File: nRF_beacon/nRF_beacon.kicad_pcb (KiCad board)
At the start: 4 copper layers, 60 x 90 mm, 69 parts, among them J1 Conn_02x05_Odd_Even, J2 Conn_02x03_Counter_Clockwise, U1 nRF54L15-QFAA, U2 NPM1300-QEAA-R7, U3 MAX98357A, U4 12BHC186P1-GR, X1 32MHz, X2 32.768 kHz

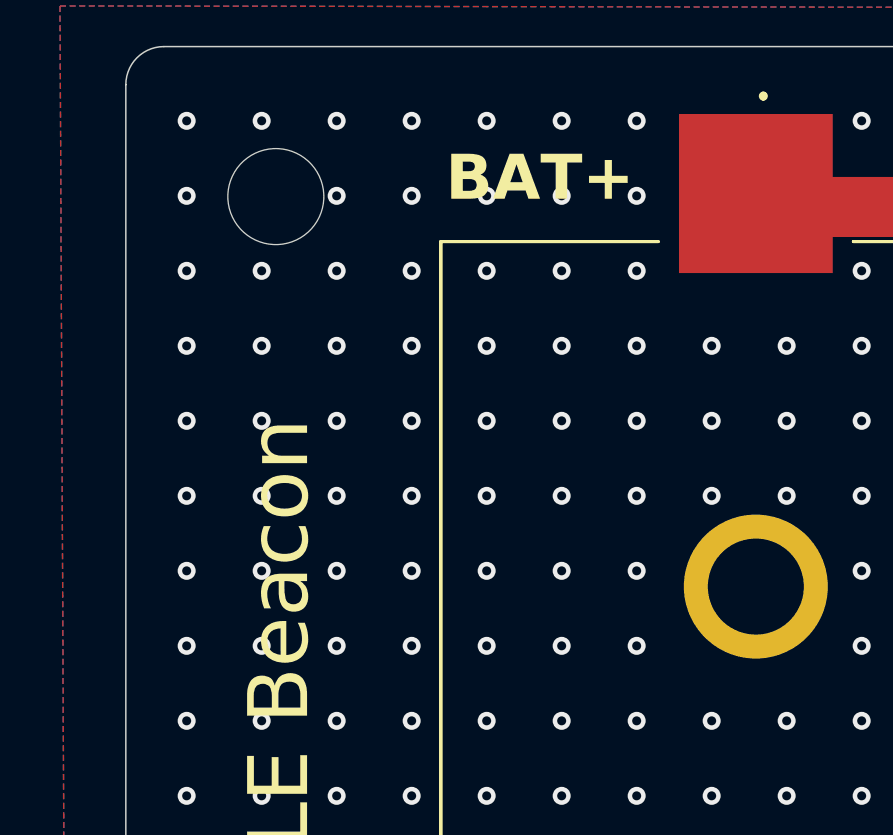
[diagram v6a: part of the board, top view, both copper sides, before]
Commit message: Added silkscreen braille, blind person logo and revision
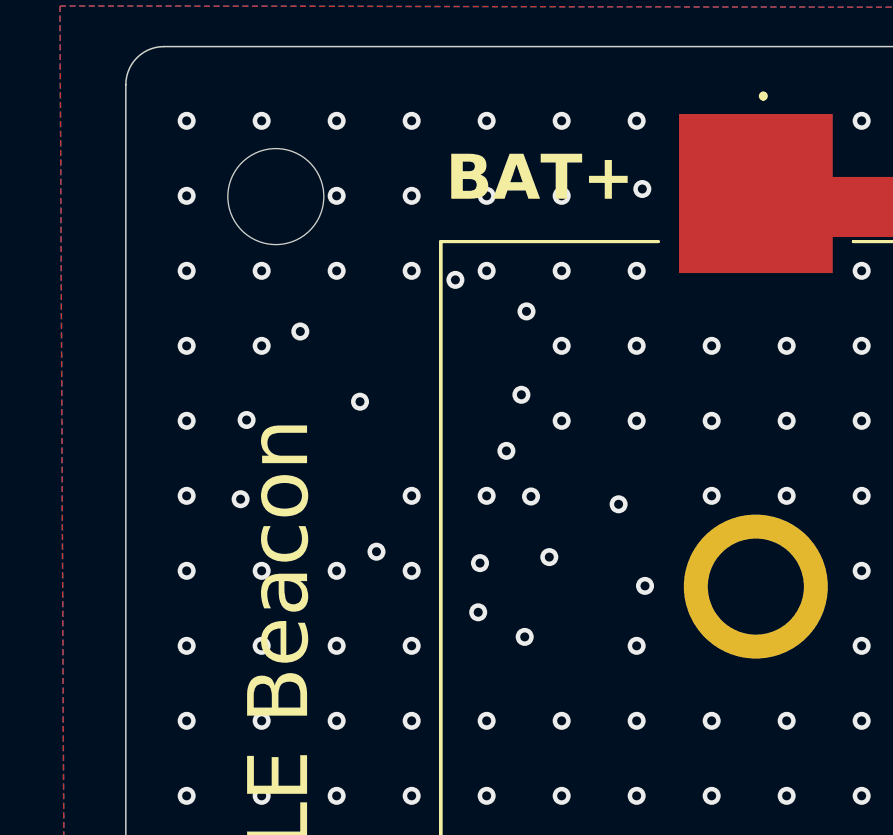
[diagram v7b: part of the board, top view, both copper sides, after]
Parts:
- added G***: LOGO, Ekse:blind, F.Cu at (147.8, 93.4)
- added G***: LOGO, Ekse:ble_sound_beacon_braille, F.Cu at (176.0, 100.0)
- added G***: LOGO, Ekse:høyttaler, F.Cu at (130.9, 69.8)
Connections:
- X1 pad 2: GND -> (no net)
- X1 pad 4: GND -> (no net)
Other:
- board text added: "BLE SOUND BEACON"
- board text added: "Layout by: Mathias Ekse"

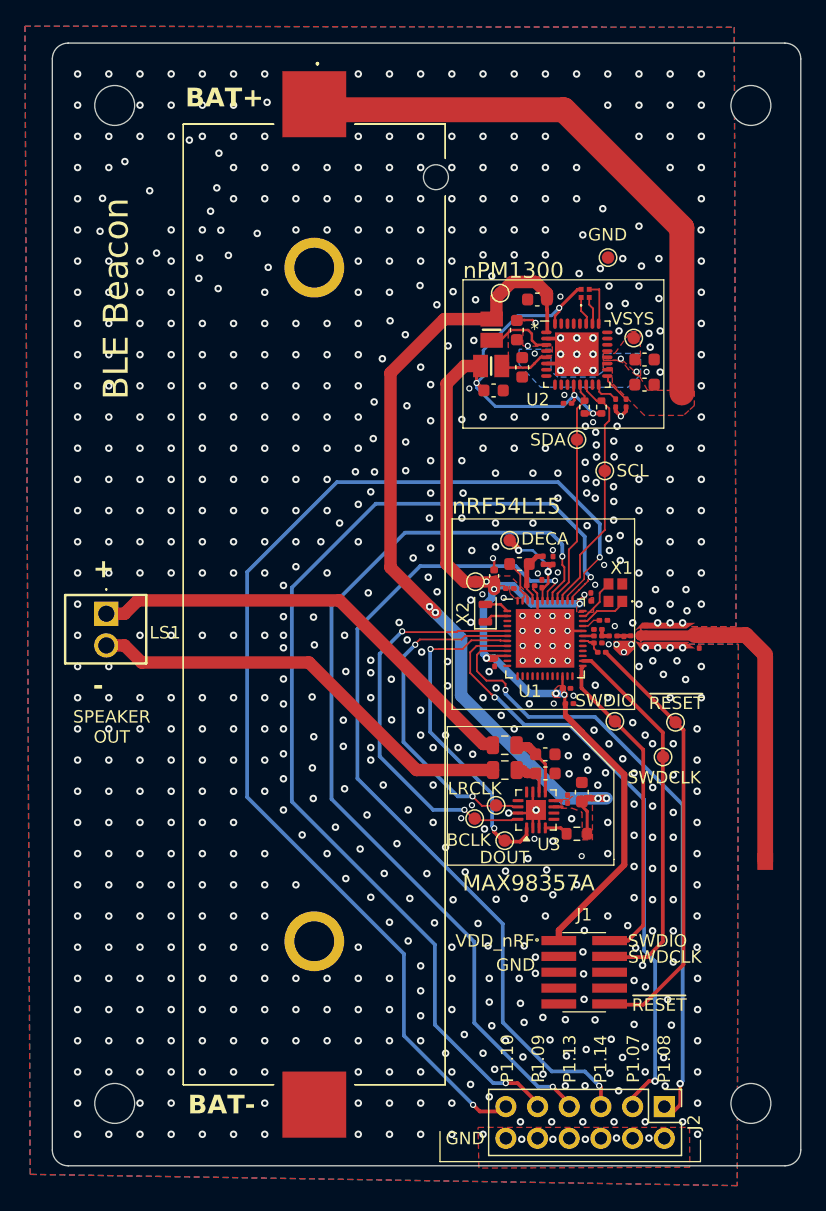
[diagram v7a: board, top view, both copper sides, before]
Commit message: Completed layout for Revision A (Prototype). Created gerber files
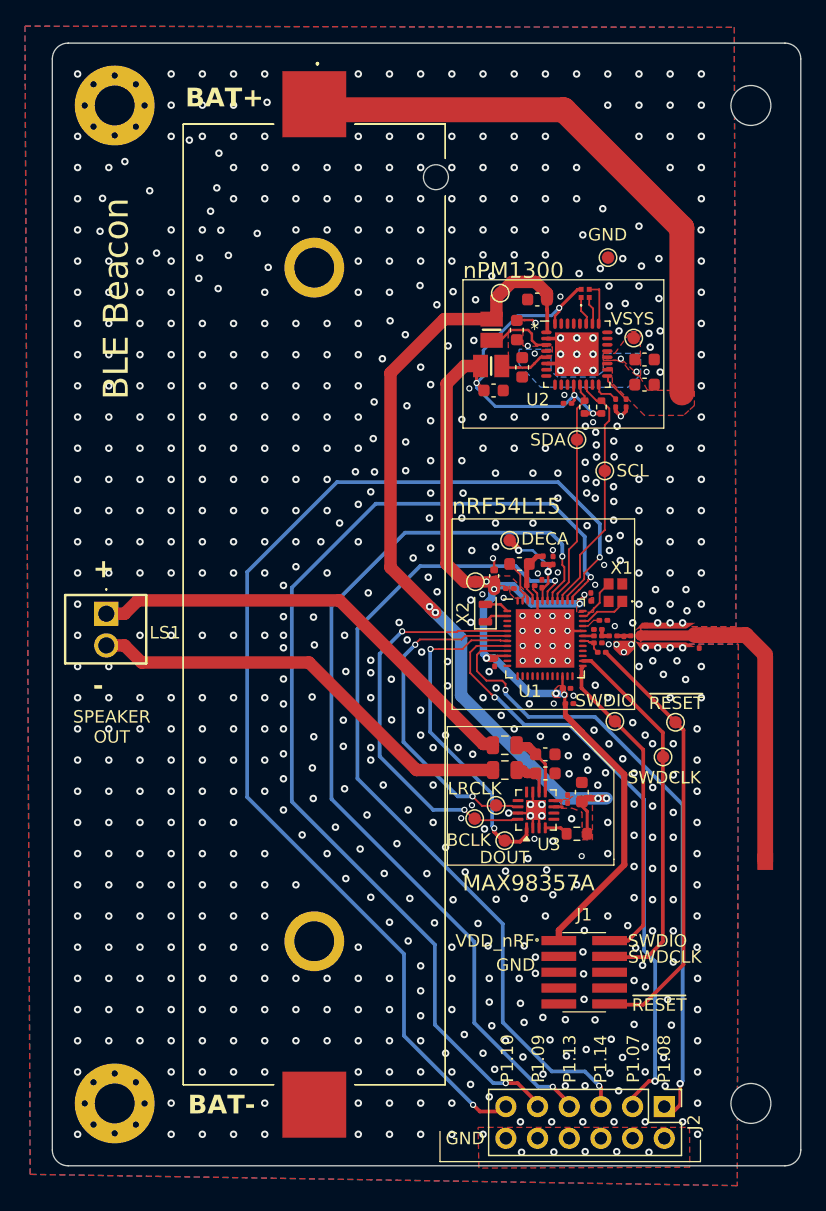
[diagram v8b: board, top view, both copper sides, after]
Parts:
- H1, H2: footprint MountingHole:MountingHole_3.2mm_M3 -> MountingHole:MountingHole_3.2mm_M3_Pad_Via
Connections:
- X1 pad 2: (no net) -> GND
- X1 pad 4: (no net) -> GND
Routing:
- net GND: vias 730 -> 721
